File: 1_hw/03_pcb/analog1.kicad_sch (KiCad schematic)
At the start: 25 parts

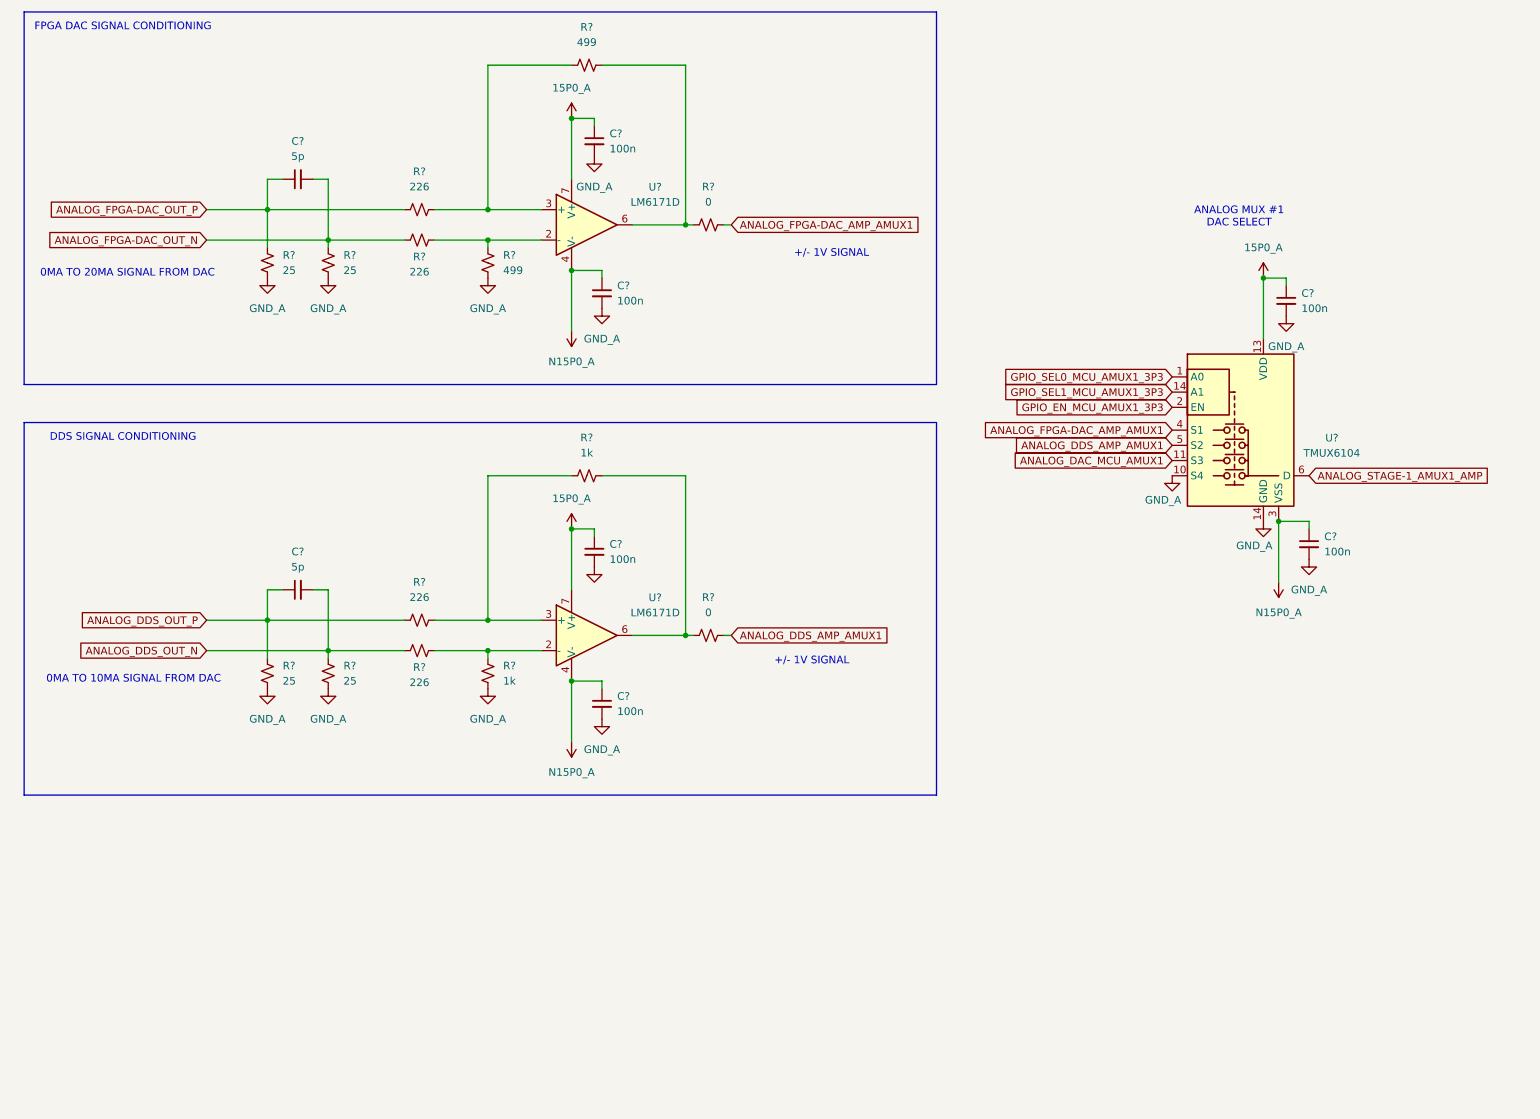
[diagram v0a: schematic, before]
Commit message: FEAT: Added Analog Stage 2 to Schematic. Some additional symbols (Pot, SPDT Analog MUX, etc.) added to Project.
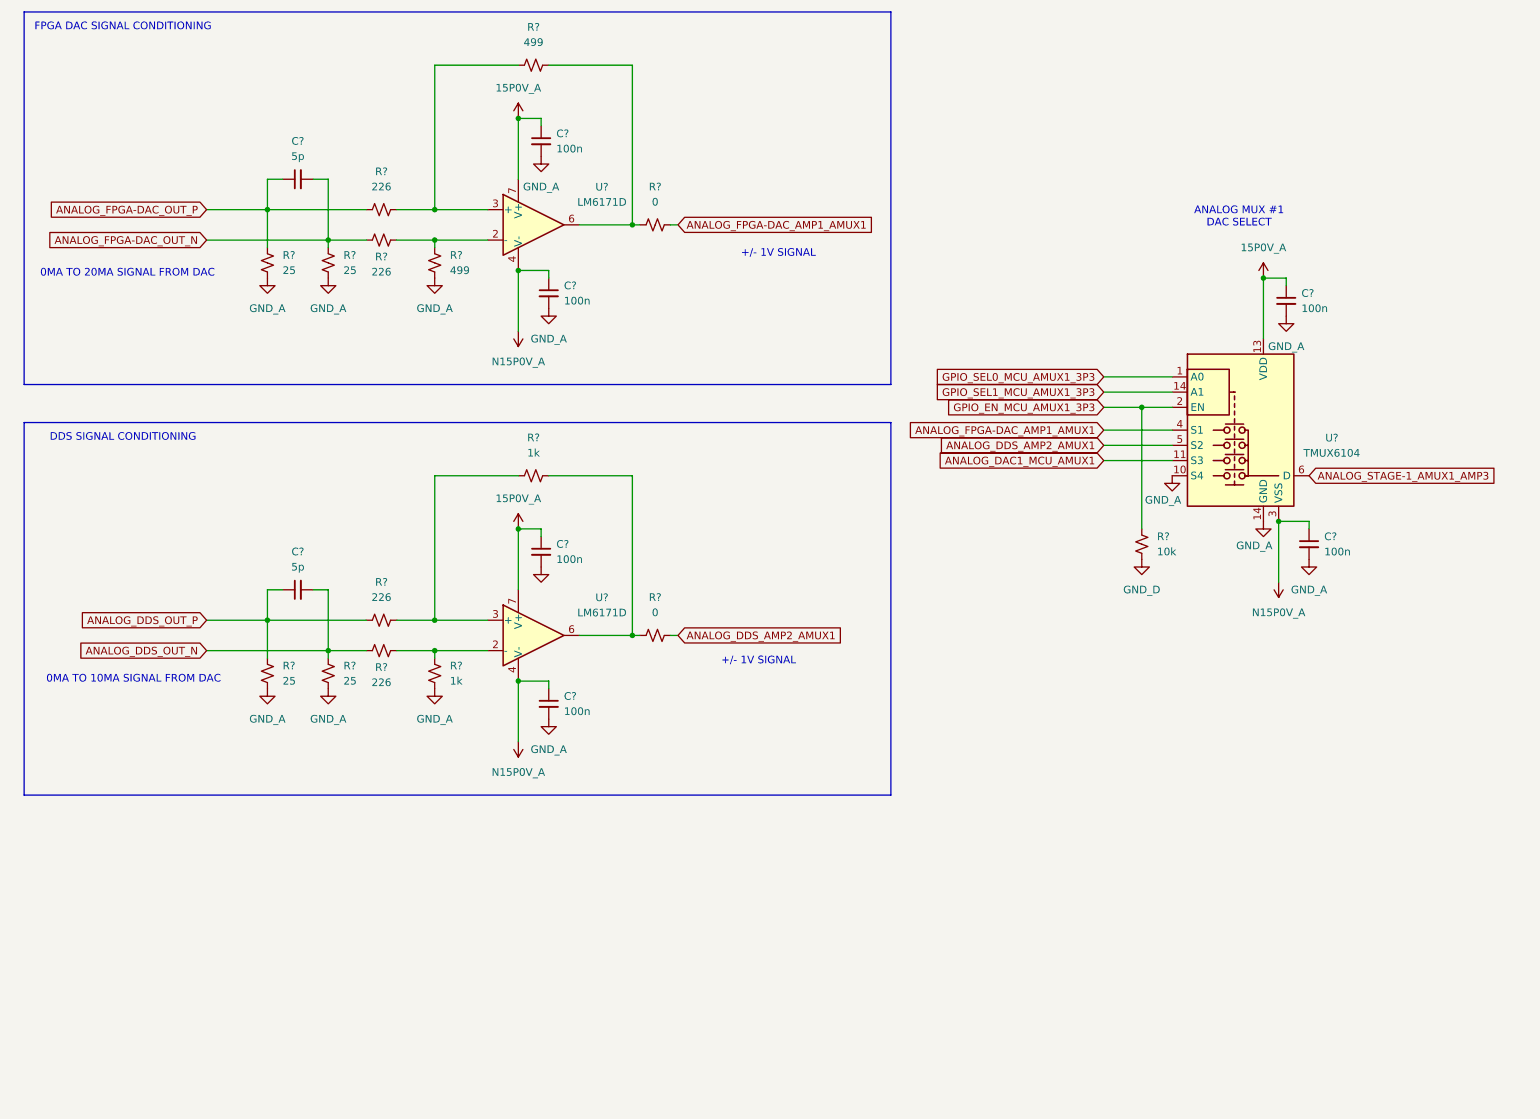
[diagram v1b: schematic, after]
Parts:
- added R?: 10k, Resistor_SMD:R_0603_1608Metric, symbol Device:R_Small_US
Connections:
- net GPIO_EN_MCU_AMUX1_3P3: now also R?.2
- net 15P0_A renamed 15P0V_A
- net ANALOG_DAC_MCU_AMUX1 renamed ANALOG_DAC1_MCU_AMUX1
- net ANALOG_DDS_AMP_AMUX1 renamed ANALOG_DDS_AMP2_AMUX1
- net ANALOG_FPGA-DAC_AMP_AMUX1 renamed ANALOG_FPGA-DAC_AMP1_AMUX1
- net ANALOG_STAGE-1_AMUX1_AMP renamed ANALOG_STAGE-1_AMUX1_AMP3
- net N15P0_A renamed N15P0V_A
- new net GND_D: R?.1
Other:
- moved on the sheet: C?, R?, U?

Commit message: FEAT: Added RVP Diode + Attenuation on the Cal Path.
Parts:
- C?: now not fitted
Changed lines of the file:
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@@
+	)
+	(rectangle
+		(start 17.78 152.4)
+		(end 157.48 200.66)
+		(stroke
+			(width 0)
+			(type default)
+		)
+		(fill
+			(type none)
+		)
 	)
 	(rectangle
@@
 		(in_bom yes)
 		(on_board yes)
-		(dnp no)
+		(dnp yes)
 		(fields_autoplaced yes)
 		(property "Reference" "C?"

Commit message: FEAT: Swapped out DDS IC and connected. Started adding Clockign Components into Schematic.
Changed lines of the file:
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@@
-	)
-	(rectangle
-		(start 17.78 152.4)
-		(end 157.48 200.66)
-		(stroke
-			(width 0)
-			(type default)
-		)
-		(fill
-			(type none)
-		)
 	)
 	(rectangle

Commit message: FEAT: Changed from two grounds (Digital + Analog) to Singular Ground IAW recommended Grounding Scheme.
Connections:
- net GND_A: no longer C?.2, C?.2, C?.2, C?.2, C?.2, R?.1, R?.1, R?.1, R?.1, R?.1, R?.1, U?.10 (S4), U?.14 (A1)
- net GND_D renamed GND
- net GND: now also C?.2, C?.2, C?.2, C?.2, C?.2, R?.1, R?.1, R?.1, R?.1, R?.1, R?.1, U?.10 (S4), U?.14 (A1)
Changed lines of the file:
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@@
 			)
 		)
-		(property "Value" "GND_A"
+		(property "Value" "GND"
 			(at 86.36 67.31 0)
 			(effects
@@
 			)
 		)
-		(property "Value" "GND_A"
+		(property "Value" "GND"
 			(at 228.6 73.66 0)
 			(effects
@@
 			)
 		)
-		(property "Value" "GND_A"
+		(property "Value" "GND"
 			(at 223.266 106.934 0)
 			(effects
@@
 			)
 		)
-		(property "Value" "GND_A"
+		(property "Value" "GND"
 			(at 208.026 99.314 0)
 			(effects
@@
 			)
 		)
-		(property "Value" "GND_A"
+		(property "Value" "GND"
 			(at 68.58 135.89 0)
 			(effects
@@
 			)
 		)
-		(property "Value" "GND_A"
+		(property "Value" "GND"
 			(at 232.41 114.3 0)
 			(effects
@@
 			)
 		)
-		(property "Value" "GND_A"
+		(property "Value" "GND"
 			(at 68.58 67.31 0)
 			(effects
@@
 			)
 		)
-		(property "Value" "GND_A"
+		(property "Value" "GND"
 			(at 58.42 67.31 0)
 			(effects
@@
 			)
 		)
-		(property "Value" "GND_D"
+		(property "Value" "GND"
 			(at 204.47 114.3 0)
 			(effects
@@
 			)
 		)
-		(property "Value" "GND_A"
+		(property "Value" "GND"
 			(at 86.36 135.89 0)
 			(effects
@@
 			)
 		)
-		(property "Value" "GND_A"
+		(property "Value" "GND"
 			(at 105.41 140.97 0)
 			(effects
@@
 			)
 		)
-		(property "Value" "GND_A"
+		(property "Value" "GND"
 			(at 58.42 135.89 0)
 			(effects
@@
 			)
 		)
-		(property "Value" "GND_A"
+		(property "Value" "GND"
 			(at 104.14 46.99 0)
 			(effects
@@
 			)
 		)
-		(property "Value" "GND_A"
+		(property "Value" "GND"
 			(at 105.41 72.39 0)
 			(effects

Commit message: FEAT: Added +15V and -15V Regulator. Replaced some Symbols to add additional Part Number Field.
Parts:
- U? (x2): Part Number (none) -> LM6171D
- U?: footprint TBD -> BRZK_TBD; Part Number (none) -> TMUX6104
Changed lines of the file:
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@@
+			)
+		)
+		(property "Part Number" "LM6171D"
+			(at 102.87 53.34 0)
+			(effects
+				(font
+					(size 1.27 1.27)
+				)
+				(hide yes)
 			)
 		)
@@
 			)
 		)
-		(property "Footprint" "TBD"
+		(property "Footprint" "BRZK_TBD"
 			(at 219.71 92.71 0)
 			(effects
@@
 			)
 		)
+		(property "Part Number" "TMUX6104"
+			(at 219.71 90.17 0)
+			(effects
+				(font
+					(size 1.27 1.27)
+				)
+				(hide yes)
+			)
+		)
 		(pin "13"
 		)
@@
 			(at 102.87 121.92 0)
 			(effects
+				(font
+					(size 1.27 1.27)
+				)
+				(hide yes)
+			)
+		)
+		(property "Part Number" "LM6171D"
+			(at 102.87 121.92 0)
+			(effects

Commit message: FEAT: Added Connectors on Schematic. Created Connector Footprints.
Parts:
- gave numbers to parts that had none: 26
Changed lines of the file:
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@@
 		(dnp no)
 		(fields_autoplaced yes)
-		(property "Reference" "R?"
+		(property "Reference" "R60"
 			(at 102.87 20.32 90)
 			(effects
@@
 			(project "arb"
 				(path "/866ef9be-3b01-4288-a6e0-a2357aa17e50/15631b2d-3708-4ae8-a4e9-7f8a7b587733"
-					(reference "R?")
+					(reference "R60")
 					(unit 1)
 				)
@@
 		(on_board yes)
 		(dnp no)
-		(property "Reference" "R?"
+		(property "Reference" "R57"
 			(at 77.47 127.254 90)
 			(effects
@@
 			(project "arb"
 				(path "/866ef9be-3b01-4288-a6e0-a2357aa17e50/15631b2d-3708-4ae8-a4e9-7f8a7b587733"
-					(reference "R?")
+					(reference "R57")
 					(unit 1)
 				)
@@
 		(dnp no)
 		(fields_autoplaced yes)
-		(property "Reference" "C?"
+		(property "Reference" "C88"
 			(at 63.5063 39.37 90)
 			(effects
@@
 			(project ""
 				(path "/866ef9be-3b01-4288-a6e0-a2357aa17e50/15631b2d-3708-4ae8-a4e9-7f8a7b587733"
-					(reference "C?")
+					(reference "C88")
 					(unit 1)
 				)
@@
 		(dnp no)
 		(fields_autoplaced yes)
-		(property "Reference" "R?"
+		(property "Reference" "R61"
 			(at 102.87 88.9 90)
 			(effects
@@
 			(project "arb"
 				(path "/866ef9be-3b01-4288-a6e0-a2357aa17e50/15631b2d-3708-4ae8-a4e9-7f8a7b587733"
-					(reference "R?")
+					(reference "R61")
 					(unit 1)
 				)
@@
 		(dnp no)
 		(fields_autoplaced yes)
-		(property "Reference" "C?"
+		(property "Reference" "C95"
 			(at 234.95 105.4163 0)
 			(effects
@@
 			(project "arb"
 				(path "/866ef9be-3b01-4288-a6e0-a2357aa17e50/15631b2d-3708-4ae8-a4e9-7f8a7b587733"
-					(reference "C?")
+					(reference "C95")
 					(unit 1)
 				)
@@
 		(dnp no)
 		(fields_autoplaced yes)
-		(property "Reference" "R?"
+		(property "Reference" "R58"
 			(at 88.9 58.4199 0)
 			(effects
@@
 			(project "arb"
 				(path "/866ef9be-3b01-4288-a6e0-a2357aa17e50/15631b2d-3708-4ae8-a4e9-7f8a7b587733"
-					(reference "R?")
+					(reference "R58")
 					(unit 1)
 				)
@@
 		(on_board yes)
 		(dnp no)
-		(property "Reference" "R?"
+		(property "Reference" "R55"
 			(at 77.47 58.674 90)
 			(effects
@@
 			(project "arb"
 				(path "/866ef9be-3b01-4288-a6e0-a2357aa17e50/15631b2d-3708-4ae8-a4e9-7f8a7b587733"
-					(reference "R?")
+					(reference "R55")
 					(unit 1)
 				)
@@
 		(dnp no)
 		(fields_autoplaced yes)
-		(property "Reference" "C?"
+		(property "Reference" "C90"
 			(at 106.68 38.1063 0)
 			(effects
@@
 			(project "arb"
 				(path "/866ef9be-3b01-4288-a6e0-a2357aa17e50/15631b2d-3708-4ae8-a4e9-7f8a7b587733"
-					(reference "C?")
+					(reference "C90")
 					(unit 1)
 				)
@@
 		(dnp no)
 		(fields_autoplaced yes)
-		(property "Reference" "C?"
+		(property "Reference" "C93"
 			(at 107.95 132.0863 0)
 			(effects
@@
 			(project "arb"
 				(path "/866ef9be-3b01-4288-a6e0-a2357aa17e50/15631b2d-3708-4ae8-a4e9-7f8a7b587733"
-					(reference "C?")
+					(reference "C93")
 					(unit 1)
 				)
@@
 		(dnp no)
 		(fields_autoplaced yes)
-		(property "Reference" "U?"
+		(property "Reference" "U18"
 			(at 114.3 47.0214 0)
 			(effects
@@
 			(project ""
 				(path "/866ef9be-3b01-4288-a6e0-a2357aa17e50/15631b2d-3708-4ae8-a4e9-7f8a7b587733"
-					(reference "U?")
+					(reference "U18")
 					(unit 1)
 				)
@@
 		(dnp no)
 		(fields_autoplaced yes)
-		(property "Reference" "R?"
+		(property "Reference" "R62"
 			(at 123.19 46.99 90)
 			(effects
@@
 			(project "arb"
 				(path "/866ef9be-3b01-4288-a6e0-a2357aa17e50/15631b2d-3708-4ae8-a4e9-7f8a7b587733"
-					(reference "R?")
+					(reference "R62")
 					(unit 1)
 				)
@@
 		(dnp yes)
 		(fields_autoplaced yes)
-		(property "Reference" "C?"
+		(property "Reference" "C89"
 			(at 63.5063 107.95 90)
 			(effects
@@
 			(project "arb"
 				(path "/866ef9be-3b01-4288-a6e0-a2357aa17e50/15631b2d-3708-4ae8-a4e9-7f8a7b587733"
-					(reference "C?")
+					(reference "C89")
 					(unit 1)
 				)
@@
 		(dnp no)
 		(fields_autoplaced yes)
-		(property "Reference" "C?"
+		(property "Reference" "C94"
 			(at 231.14 64.7763 0)
 			(effects
@@
 			(project "arb"
 				(path "/866ef9be-3b01-4288-a6e0-a2357aa17e50/15631b2d-3708-4ae8-a4e9-7f8a7b587733"
-					(reference "C?")
+					(reference "C94")
 					(unit 1)
 				)
@@
 		(dnp no)
 		(fields_autoplaced yes)
-		(property "Reference" "R?"
+		(property "Reference" "R50"
 			(at 60.96 58.4199 0)
 			(effects
@@
 			(project "arb"
 				(path "/866ef9be-3b01-4288-a6e0-a2357aa17e50/15631b2d-3708-4ae8-a4e9-7f8a7b587733"
-					(reference "R?")
+					(reference "R50")
 					(unit 1)
 				)
@@
 		(dnp no)
 		(fields_autoplaced yes)
-		(property "Reference" "R?"
+		(property "Reference" "R53"
 			(at 71.12 126.9999 0)
 			(effects
@@
 			(project "arb"
 				(path "/866ef9be-3b01-4288-a6e0-a2357aa17e50/15631b2d-3708-4ae8-a4e9-7f8a7b587733"
-					(reference "R?")
+					(reference "R53")
 					(unit 1)
 				)
@@
 		(dnp no)
 		(fields_autoplaced yes)
-		(property "Reference" "R?"
+		(property "Reference" "R64"
 			(at 207.01 105.4099 0)
 			(effects
@@
 			(project "arb"
 				(path "/866ef9be-3b01-4288-a6e0-a2357aa17e50/15631b2d-3708-4ae8-a4e9-7f8a7b587733"
-					(reference "R?")
+					(reference "R64")
 					(unit 1)
 				)
@@
 		(on_board yes)
 		(dnp no)
-		(property "Reference" "U?"
+		(property "Reference" "U20"
 			(at 236.22 88.9314 0)
 			(effects
@@
 			(project ""
 				(path "/866ef9be-3b01-4288-a6e0-a2357aa17e50/15631b2d-3708-4ae8-a4e9-7f8a7b587733"
-					(reference "U?")
+					(reference "U20")
 					(unit 1)
 				)
@@
 		(dnp no)
 		(fields_autoplaced yes)
-		(property "Reference" "R?"
+		(property "Reference" "R56"
 			(at 77.47 113.03 90)
 			(effects
@@
 			(project "arb"
 				(path "/866ef9be-3b01-4288-a6e0-a2357aa17e50/15631b2d-3708-4ae8-a4e9-7f8a7b587733"
-					(reference "R?")
+					(reference "R56")
 					(unit 1)
 				)
@@
 		(dnp no)
 		(fields_autoplaced yes)
-		(property "Reference" "C?"
+		(property "Reference" "C91"
 			(at 106.68 106.6863 0)
 			(effects
@@
 			(project "arb"
 				(path "/866ef9be-3b01-4288-a6e0-a2357aa17e50/15631b2d-3708-4ae8-a4e9-7f8a7b587733"
-					(reference "C?")
+					(reference "C91")
 					(unit 1)
 				)
@@
 		(dnp no)
 		(fields_autoplaced yes)
-		(property "Reference" "C?"
+		(property "Reference" "C92"
 			(at 107.95 63.5063 0)
 			(effects
@@
 			(project "arb"
 				(path "/866ef9be-3b01-4288-a6e0-a2357aa17e50/15631b2d-3708-4ae8-a4e9-7f8a7b587733"
-					(reference "C?")
+					(reference "C92")
 					(unit 1)
 				)
@@
 		(dnp no)
 		(fields_autoplaced yes)
-		(property "Reference" "R?"
+		(property "Reference" "R59"
 			(at 88.9 126.9999 0)
 			(effects
@@
 			(project "arb"
 				(path "/866ef9be-3b01-4288-a6e0-a2357aa17e50/15631b2d-3708-4ae8-a4e9-7f8a7b587733"
-					(reference "R?")
+					(reference "R59")
 					(unit 1)
 				)
@@
 		(dnp no)
 		(fields_autoplaced yes)
-		(property "Reference" "R?"
+		(property "Reference" "R52"
 			(at 71.12 58.4199 0)
 			(effects
@@
 			(project "arb"
 				(path "/866ef9be-3b01-4288-a6e0-a2357aa17e50/15631b2d-3708-4ae8-a4e9-7f8a7b587733"
-					(reference "R?")
+					(reference "R52")
 					(unit 1)
 				)
@@
 		(dnp no)
 		(fields_autoplaced yes)
-		(property "Reference" "U?"
+		(property "Reference" "U19"
 			(at 114.3 115.6014 0)
 			(effects
@@
 			(project "arb"
 				(path "/866ef9be-3b01-4288-a6e0-a2357aa17e50/15631b2d-3708-4ae8-a4e9-7f8a7b587733"
-					(reference "U?")
+					(reference "U19")
 					(unit 1)
 				)
@@
 		(dnp no)
 		(fields_autoplaced yes)
-		(property "Reference" "R?"
+		(property "Reference" "R51"
 			(at 60.96 126.9999 0)
 			(effects
@@
 			(project "arb"
 				(path "/866ef9be-3b01-4288-a6e0-a2357aa17e50/15631b2d-3708-4ae8-a4e9-7f8a7b587733"
-					(reference "R?")
+					(reference "R51")
 					(unit 1)
 				)
@@
 		(dnp no)
 		(fields_autoplaced yes)
-		(property "Reference" "R?"
+		(property "Reference" "R54"
 			(at 77.47 44.45 90)
 			(effects
@@
 			(project ""
 				(path "/866ef9be-3b01-4288-a6e0-a2357aa17e50/15631b2d-3708-4ae8-a4e9-7f8a7b587733"
-					(reference "R?")
+					(reference "R54")
 					(unit 1)
 				)
@@
 		(dnp no)
 		(fields_autoplaced yes)
-		(property "Reference" "R?"
+		(property "Reference" "R63"
 			(at 123.19 115.57 90)
 			(effects
@@
 			(project "arb"
 				(path "/866ef9be-3b01-4288-a6e0-a2357aa17e50/15631b2d-3708-4ae8-a4e9-7f8a7b587733"
-					(reference "R?")
+					(reference "R63")
 					(unit 1)
 				)

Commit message: FEAT: Assigned Reference Designators; Assigned Passives Part Numbers & Footprints (0603); Assigned LCSC P/Ns.
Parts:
- C88, C89: footprint (none) -> Capacitor_SMD:C_0603_1608Metric; LCSC (none) -> C327203; Part Number (none) -> CC0603CRNPO9BN5R0
- C90, C91, C92, C93, C94, C95: LCSC (none) -> C24452; PN CL10B104JB8NNNC -> (none); Part Number (none) -> CL10B104JB8NNNC
- R51: renamed from R50; value 25 -> 24.9; footprint (none) -> Resistor_SMD:R_0603_1608Metric; LCSC (none) -> C22916; Part Number (none) -> 0603WAF249JT5E
- R52: renamed from R51; value 25 -> 24.9; footprint (none) -> Resistor_SMD:R_0603_1608Metric; LCSC (none) -> C22916; Part Number (none) -> 0603WAF249JT5E
- R53: renamed from R52; value 25 -> 24.9; footprint (none) -> Resistor_SMD:R_0603_1608Metric; LCSC (none) -> C22916; Part Number (none) -> 0603WAF249JT5E
- R54: renamed from R53; value 25 -> 24.9; footprint (none) -> Resistor_SMD:R_0603_1608Metric; LCSC (none) -> C22916; Part Number (none) -> 0603WAF249JT5E
- R55: renamed from R54; footprint (none) -> Resistor_SMD:R_0603_1608Metric; LCSC (none) -> C861234; Part Number (none) -> RT0603BRD07226RL
- R56: renamed from R55; footprint (none) -> Resistor_SMD:R_0603_1608Metric; LCSC (none) -> C861234; Part Number (none) -> RT0603BRD07226RL
- R57: renamed from R56; footprint (none) -> Resistor_SMD:R_0603_1608Metric; LCSC (none) -> C861234; Part Number (none) -> RT0603BRD07226RL
- R58: renamed from R57; footprint (none) -> Resistor_SMD:R_0603_1608Metric; LCSC (none) -> C861234; Part Number (none) -> RT0603BRD07226RL
- R59: renamed from R58; footprint (none) -> Resistor_SMD:R_0603_1608Metric; LCSC (none) -> C23065; Part Number (none) -> 0603WAF4990T5E
- R60: renamed from R59; footprint (none) -> Resistor_SMD:R_0603_1608Metric; LCSC (none) -> C22548; Part Number (none) -> RC0603FR-071KL
- R61: renamed from R60; footprint (none) -> Resistor_SMD:R_0603_1608Metric; LCSC (none) -> C23065; Part Number (none) -> 0603WAF4990T5E
- R62: renamed from R61; footprint (none) -> Resistor_SMD:R_0603_1608Metric; LCSC (none) -> C22548; Part Number (none) -> RC0603FR-071KL
- R63: renamed from R62; LCSC (none) -> C15402; PN 0603WAJ0000T5E -> (none); Part Number (none) -> 0603WAJ0000T5E
- R64: renamed from R63; LCSC (none) -> C15402; PN 0603WAJ0000T5E -> (none); Part Number (none) -> 0603WAJ0000T5E
- R65: renamed from R64; LCSC (none) -> C25804; PN CR-03FC7---10K -> (none); Part Number (none) -> 0603WAF1002T5E
- U18, U19: value LM6171D -> LM6171; symbol BRZK_OPAMP:LM6171D -> BRZK_OPAMP:LM6171; LCSC (none) -> C2058493; Part Number LM6171D -> LM6171BIMX/NOPB
- U20: footprint BRZK_TBD -> (none); LCSC (none) -> C2673388; Part Number TMUX6104 -> TMUX6104PWR

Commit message: FEAT: Added MCU Flash. Finished creating & assigning footprints. Ran ERC & cleared out issues. Ready for Layout.
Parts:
- removed U20: TMUX6104, symbol BRZK_MUX:TMUX6104
- added U21: TMUX6104, Package_SO:TSSOP-14_4.4x5mm_P0.65mm, symbol BRZK_MUX:TMUX6104
- renumbered C88 to C89, C89 to C90, C90 to C91, C91 to C92, C92 to C93, C93 to C94, C94 to C95, C95 to C96, R51 to R57, R52 to R58, R53 to R59, R54 to R60, R55 to R61, R56 to R62, R57 to R63, R58 to R64, R59 to R65, R60 to R66, R61 to R67, R62 to R68, R63 to R69, R64 to R70, R65 to R71, U18 to U19, U19 to U20
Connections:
- net GND_A is gone; now on net GND: C92.2
- net 15P0V_A: now also U21.13 (VDD)
- net ANALOG_DAC1_MCU_AMUX1: now also U21.11 (S3)
- net ANALOG_DDS_AMP2_AMUX1: now also U21.5 (S2)
- net ANALOG_FPGA-DAC_AMP1_AMUX1: now also U21.4 (S1)
- net ANALOG_STAGE-1_AMUX1_AMP3: now also U21.6 (D)
- net GND: now also U21.10 (S4), U21.14 (A1)
- net GPIO_EN_MCU_AMUX1_3P3: now also U21.2 (EN)
- net GPIO_SEL0_MCU_AMUX1_3P3: now also U21.1 (A0)
- net GPIO_SEL1_MCU_AMUX1_3P3: now also U21.14 (A1)
- net N15P0V_A: now also U21.3 (VSS)
- new net: U21.7 (NC), U21.8 (NC), U21.9 (NC)
